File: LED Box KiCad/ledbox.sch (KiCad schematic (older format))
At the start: 23 parts

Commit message: LED Vorwiderstände auf E-Reihen angepasst
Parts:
- R?: value 185 -> 180
- R?: value 58 -> 56
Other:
- note added: "! rund 150mW !"
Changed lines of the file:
@@
 P 8300 1950
 F 0 "R?" V 8380 1950 50  0000 C CNN
-F 1 "185" V 8300 1950 50  0000 C CNN
+F 1 "180" V 8300 1950 50  0000 C CNN
 F 2 "" V 8230 1950 50  0001 C CNN
 F 3 "" H 8300 1950 50  0001 C CNN
@@
 P 8800 1950
 F 0 "R?" V 8880 1950 50  0000 C CNN
-F 1 "58" V 8800 1950 50  0000 C CNN
+F 1 "56" V 8800 1950 50  0000 C CNN
 F 2 "" V 8730 1950 50  0001 C CNN
 F 3 "" H 8800 1950 50  0001 C CNN
@@
 Wire Wire Line
 	6000 4100 6000 4000
+Text Notes 8700 2350 1    60   ~ 0
+! rund 150mW !
 $EndSCHEMATC

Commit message: Ordner plot in output geändert. BOM hinzugefügt
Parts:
- gave numbers to parts that had none: 23

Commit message: Version 1.1: - RGB LED Symbol angepasst - Button und IR LED auf eine vierer Klemmleiste Footprints assoziiert
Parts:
- removed D1: LED_IR, symbol LED
- removed D2: LED_RGB, symbol LED_RGB
- removed J2: Button, symbol Conn_01x02
- added D1: LRTBG6TG, ledbox-newfootprints:LED-6-BIG, symbol LRTBG6TG
- added J2: BTN_IR, ledbox-newfootprints:METZ-SR21304VBNC, symbol Conn_01x04
- C1, C2, C3, C4: footprint (none) -> Capacitors_SMD:C_1206
- C5: footprint (none) -> Capacitors_SMD:CP_Elec_4x5.7
- CON1: value AVR-ISP-6 -> AVR_ISP; footprint AVR-ISP-6 -> Pin_Headers:Pin_Header_Straight_2x03
- J1: value Conn_02x05_Odd_Even -> Bus; footprint (none) -> Pin_Headers:Pin_Header_Straight_2x05
- R1, R2, R3, R4, R5, R6, R7, R8, R9: footprint (none) -> Resistors_SMD:R_1206
- U1: footprint Housings_DIP:DIP-20_W7.62mm -> Housings_SOIC:SOIC-20W_7.5x12.8mm_Pitch1.27mm
- U3: footprint (none) -> Housings_SOIC:SOIC-16_3.9x9.9mm_Pitch1.27mm
- Y1: footprint (none) -> Crystals:Crystal_HC49-SD_SMD
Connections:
- net labels added: IR_LED_DRV
- wire segments 92 -> 93
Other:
- note added: "Button"
- note added: "IR LED"
- moved on the sheet: R9

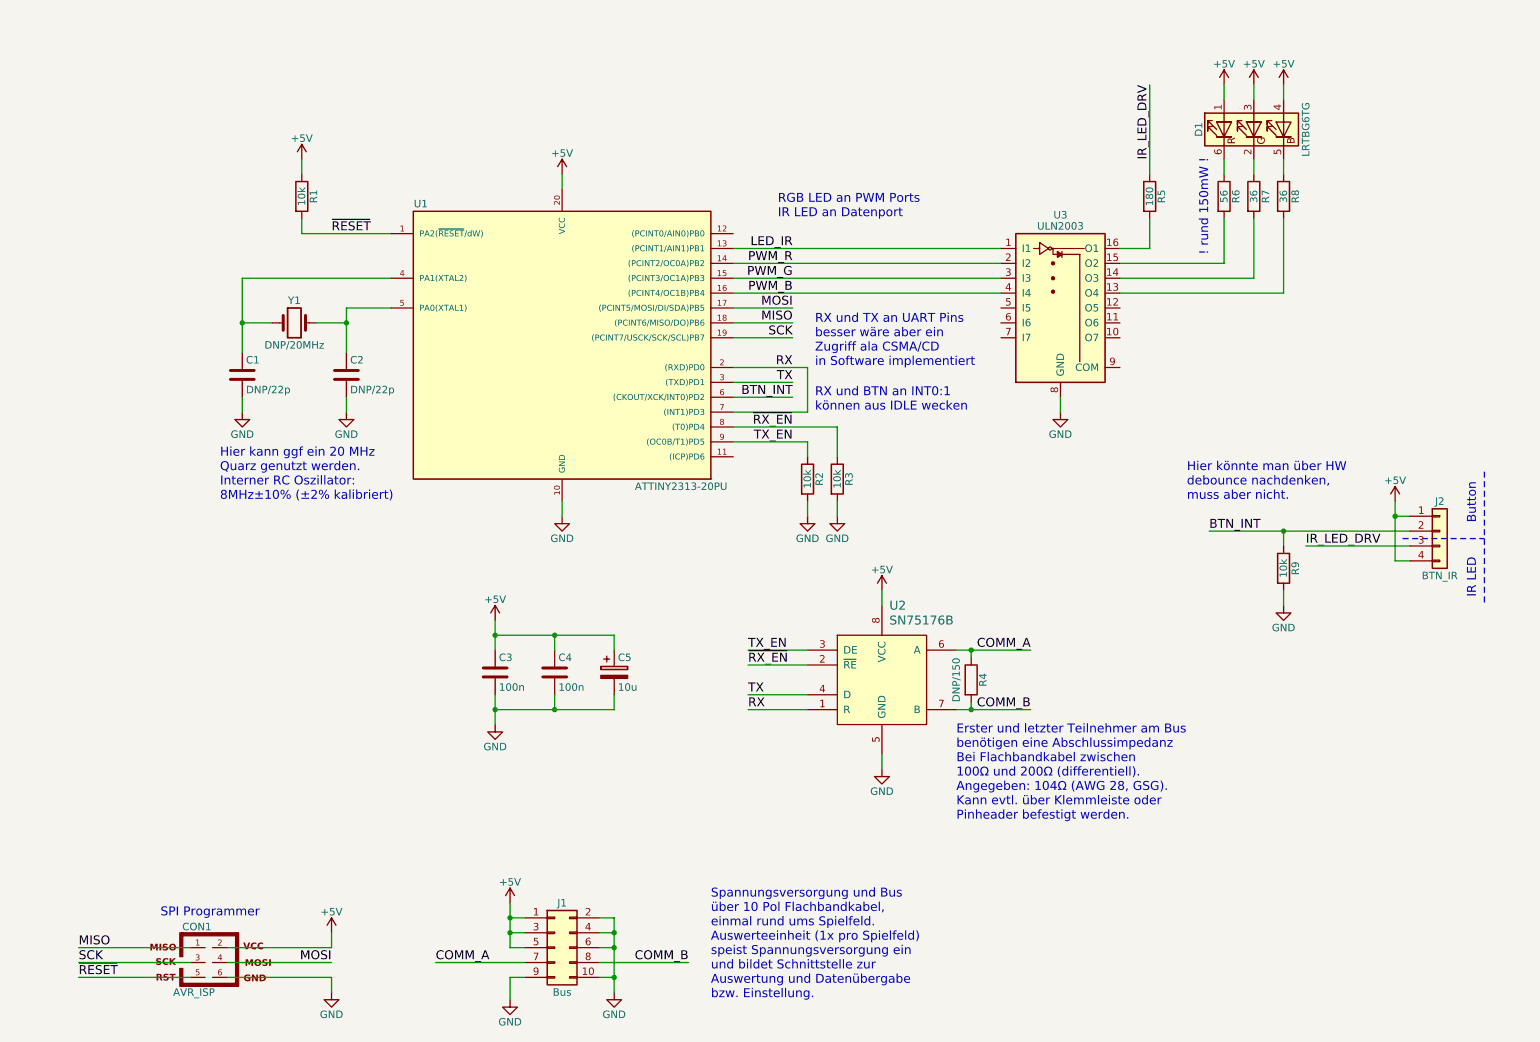
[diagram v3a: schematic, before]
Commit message: Version 2 - Anforderungen für Software hinzugefügt - CSMA/CA anstatt CSMA/CD - Kollisionsdetektion hinzugefügt - Verbinder für IR LED und Button getrennt und unterschiedlich gemacht - zusätzlicher Anschluss für Spannungsversorgung
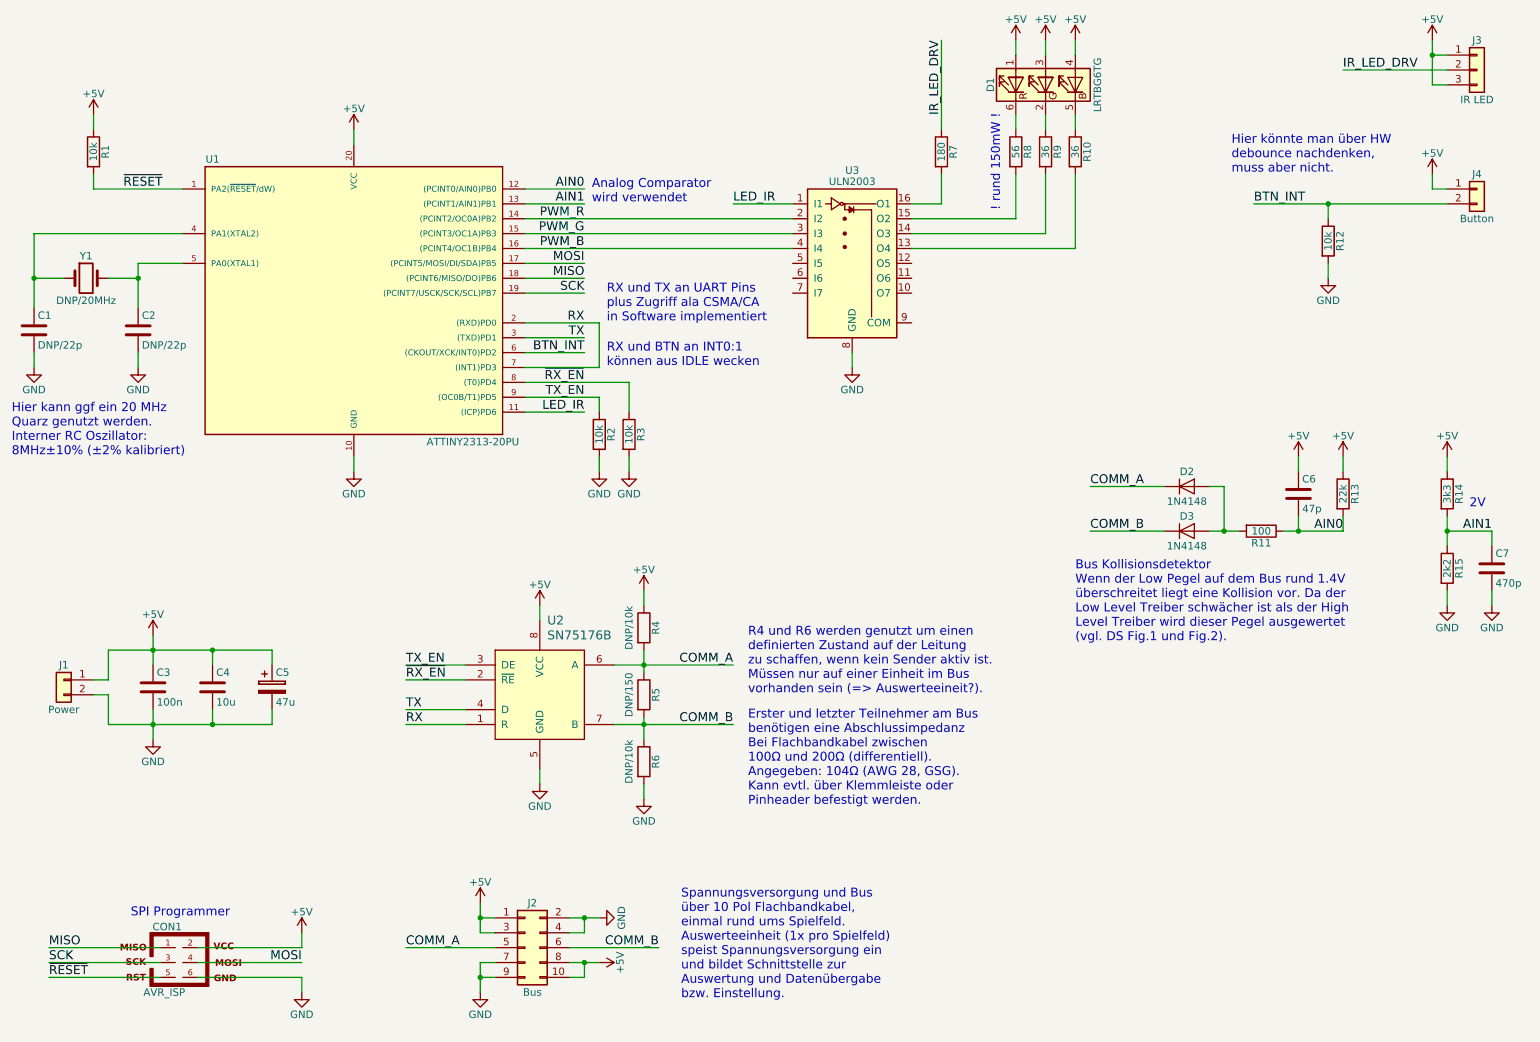
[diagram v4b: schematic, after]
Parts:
- removed J2: BTN_IR, ledbox-newfootprints:METZ-SR21304VBNC, symbol Conn_01x04
- added C6: 47p, Capacitors_SMD:C_1206, symbol C
- added C7: 470p, Capacitors_SMD:C_1206, symbol C
- added D2, D3: 1N4148, Diodes_SMD:D_MiniMELF, symbol D
- added J1: Power, Connectors_Terminal_Blocks:TerminalBlock_Pheonix_MKDS1.5-2pol, symbol Conn_01x02
- added J3: IR LED, Pin_Headers:Pin_Header_Straight_1x03, symbol Conn_01x03
- added J4: Button, Pin_Headers:Pin_Header_Straight_1x02, symbol Conn_01x02
- added R11: 100, Resistors_SMD:R_1206, symbol R
- added R13: 22k, Resistors_SMD:R_1206, symbol R
- added R14: 3k3, Resistors_SMD:R_1206, symbol R
- added R15: 2k2, Resistors_SMD:R_1206, symbol R
- added R4, R6: DNP/10k, Resistors_SMD:R_1206, symbol R
- C4: value 100n -> 10u
- C5: value 10u -> 47u
- renumbered J1 to J2, R8 to R10, R9 to R12, R4 to R5, R5 to R7, R6 to R8, R7 to R9
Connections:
- net +5V: now also J2.10 (Pin_10), J2.8 (Pin_8), C6.1, J1.1 (Pin_1), J3.1 (Pin_1), J3.3 (Pin_3), J4.1 (Pin_1), R13.1, R14.1, R4.1; no longer J2.5 (Pin_5)
- net BTN_INT: now also J4.2 (Pin_2)
- net COMM_A: now also J2.5 (Pin_5), D2.1 (K), R4.2; no longer J2.7 (Pin_7)
- net COMM_B: now also J2.6 (Pin_6), D3.1 (K), R6.1; no longer J2.8 (Pin_8)
- net GND: now also J2.7 (Pin_7), C7.2, J1.2 (Pin_2), R15.2, R6.2; no longer J2.10 (Pin_10), J2.6 (Pin_6)
- net IR_LED_DRV: now also J3.2 (Pin_2)
- net LED_IR: now also U1.11 ((ICP)PD6); no longer U1.13 ((PCINT1/AIN1)PB1)
- net AIN0: now reaches U1.12 ((PCINT0/AIN0)PB0)
- net AIN0: now also C6.2, R11.1, R13.2
- new net: D2.2 (A), D3.2 (A), R11.2
- new net AIN1: C7.1, R14.2, R15.1, U1.13 ((PCINT1/AIN1)PB1)
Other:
- note added: "2V"
- note added: "Analog Comparator \nwird verwendet"
- note added: "Bus Kollisionsdetektor\nWenn der Low Pegel auf dem Bus rund 1.4V \nüberschreitet liegt eine Kollision vor. Da der \nLow Level Treiber schwächer ist als der High \nLevel Treiber wird dieser Pegel ausgewertet \n(vgl. DS Fig.1 und Fig.2)."
- note added: "R4 und R6 werden genutzt um einen \ndefinierten Zustand auf der Leitung \nzu schaffen, wenn kein Sender aktiv ist.\nMüssen nur auf einer Einheit im Bus \nvorhanden sein (=> Auswerteeineit?)."
- note added: "RX und TX an UART Pins\nplus Zugriff ala CSMA/CA\nin Software implementiert"
- note removed: "Button"
- note removed: "IR LED"
- note removed: "RGB LED an PWM Ports\nIR LED an Datenport"
- note removed: "RX und TX an UART Pins\nbesser wäre aber ein \nZugriff ala CSMA/CD\nin Software implementiert"
- moved on the sheet: C1, C2, C3, C4, C5, CON1, D1, J2, R1, R10, R12, R2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

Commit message: Exchanged SN75176B with ST485C
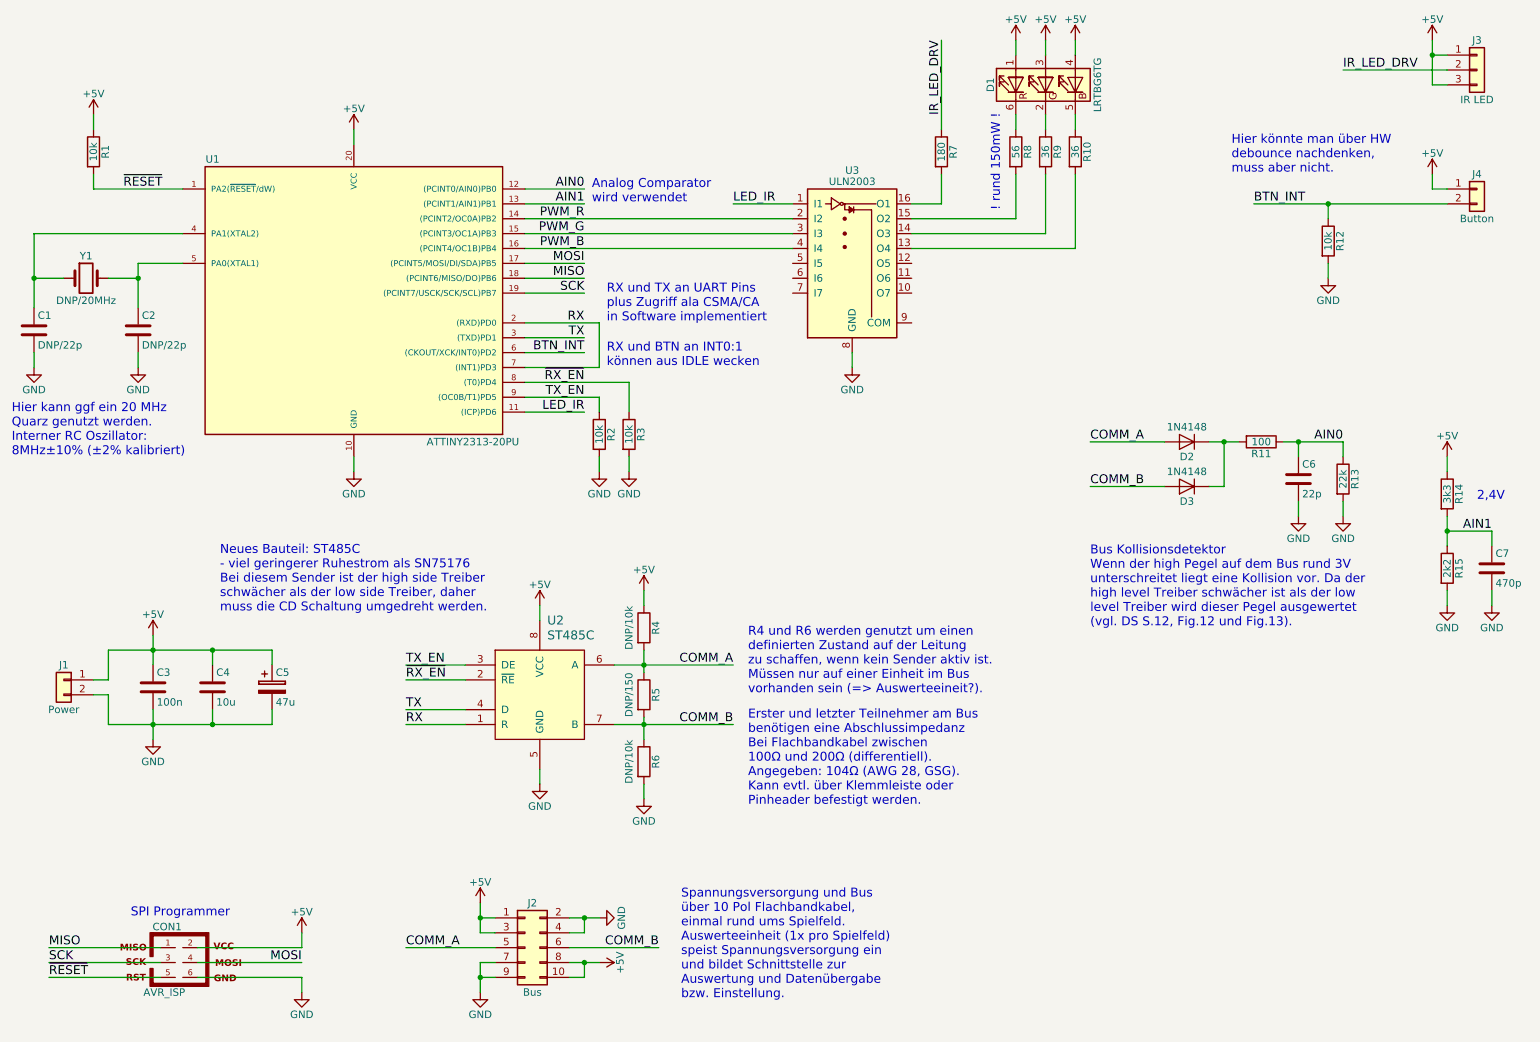
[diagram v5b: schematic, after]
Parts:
- C6: value 47p -> 22p
- U2: value SN75176B -> ST485C
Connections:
- net +5V: no longer C6.1, R13.1
- net AIN0: now also C6.1, R13.1; no longer C6.2, R13.2
- net COMM_A: now also D2.2 (A); no longer D2.1 (K)
- net COMM_B: now also D3.2 (A); no longer D3.1 (K)
- net GND: now also C6.2, R13.2
- new net: D2.1 (K), D3.1 (K), R11.2
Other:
- note added: "2,4V"
- note added: "Bus Kollisionsdetektor\nWenn der high Pegel auf dem Bus rund 3V \nunterschreitet liegt eine Kollision vor. Da der \nhigh level Treiber schwächer ist als der low \nlevel Treiber wird dieser Pegel ausgewertet \n(vgl. DS S.12, Fig.12 und Fig.13)."
- note added: "Neues Bauteil: ST485C \n- viel geringerer Ruhestrom als SN75176 \nBei diesem Sender ist der high side Treiber \nschwächer als der low side Treiber, daher \nmuss die CD Schaltung umgedreht werden.\n"
- note removed: "2V"
- note removed: "Bus Kollisionsdetektor\nWenn der Low Pegel auf dem Bus rund 1.4V \nüberschreitet liegt eine Kollision vor. Da der \nLow Level Treiber schwächer ist als der High \nLevel Treiber wird dieser Pegel ausgewertet \n(vgl. DS Fig.1 und Fig.2)."
- moved on the sheet: C6, D2, D3, R11, R13
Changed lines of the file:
@@
 P 4200 5300
 F 0 "U2" H 4250 5800 60  0000 L CNN
-F 1 "SN75176B" H 4250 5700 60  0000 L CNN
+F 1 "ST485C" H 4250 5700 60  0000 L CNN
 F 2 "Housings_SOIC:SOIC-8_3.9x4.9mm_Pitch1.27mm" H 4250 5900 60  0001 L CNN
-F 3 "http://www.ti.com/lit/ds/symlink/sn65176b.pdf" H 4250 6000 60  0001 L CNN
+F 3 "http://www.st.com/content/ccc/resource/technical/document/datasheet/4b/81/a8/cd/8a/72/47/82/CD00002183.pdf/files/CD00002183.pdf/jcr:content/translations/en.CD00002183.pdf" H 4250 6000 60  0001 L CNN
 	1    4200 5300
 	1    0    0    -1
@@
 Wire Wire Line
 	4500 3400 4100 3400
+Text Label 7900 3600 0    60   ~ 0
+COMM_A
 Text Label 7900 3900 0    60   ~ 0
-COMM_A
-Text Label 7900 4200 0    60   ~ 0
 COMM_B
 $Comp
 L D D2
 U 1 1 59D7F0C6
+P 8550 3600
+F 0 "D2" H 8550 3700 50  0000 C CNN
+F 1 "1N4148" H 8550 3500 50  0000 C CNN
+F 2 "Diodes_SMD:D_MiniMELF" H 8550 3600 50  0001 C CNN
+F 3 "" H 8550 3600 50  0001 C CNN
+	1    8550 3600
+	-1   0    0    1
+$EndComp
+$Comp
+L D D3
+U 1 1 59D7F13F
 P 8550 3900
-F 0 "D2" H 8550 4000 50  0000 C CNN
+F 0 "D3" H 8550 4000 50  0000 C CNN
 F 1 "1N4148" H 8550 3800 50  0000 C CNN
 F 2 "Diodes_SMD:D_MiniMELF" H 8550 3900 50  0001 C CNN
 F 3 "" H 8550 3900 50  0001 C CNN
 	1    8550 3900
-	1    0    0    -1
-$EndComp
-$Comp
-L D D3
-U 1 1 59D7F13F
-P 8550 4200
-F 0 "D3" H 8550 4300 50  0000 C CNN
-F 1 "1N4148" H 8550 4100 50  0000 C CNN
-F 2 "Diodes_SMD:D_MiniMELF" H 8550 4200 50  0001 C CNN
-F 3 "" H 8550 4200 50  0001 C CNN
-	1    8550 4200
-	1    0    0    -1
-$EndComp
-Wire Wire Line
-	7900 4200 8400 4200
-Wire Wire Line
-	8400 3900 7900 3900
-Wire Wire Line
-	8700 4200 8900 4200
-Wire Wire Line
-	8800 4200 8800 3900
-Wire Wire Line
-	8800 3900 8700 3900
+	-1   0    0    1
+$EndComp
+Wire Wire Line
+	7900 3900 8400 3900
+Wire Wire Line
+	8400 3600 7900 3600
+Wire Wire Line
+	8700 3900 8800 3900
+Wire Wire Line
+	8800 3900 8800 3600
+Wire Wire Line
+	8700 3600 8900 3600
 $Comp
 L R R11
 U 1 1 59D7F58B
-P 9050 4200
-F 0 "R11" V 9130 4200 50  0000 C CNN
-F 1 "100" V 9050 4200 50  0000 C CNN
-F 2 "Resistors_SMD:R_1206" V 8980 4200 50  0001 C CNN
-F 3 "" H 9050 4200 50  0001 C CNN
-	1    9050 4200
+P 9050 3600
+F 0 "R11" V 9130 3600 50  0000 C CNN
+F 1 "100" V 9050 3600 50  0000 C CNN
+F 2 "Resistors_SMD:R_1206" V 8980 3600 50  0001 C CNN
+F 3 "" H 9050 3600 50  0001 C CNN
+	1    9050 3600
 	0    1    1    0
 $EndComp
@@
 L C C6
 U 1 1 59D7F6C9
-P 9300 3950
-F 0 "C6" H 9325 4050 50  0000 L CNN
-F 1 "47p" H 9325 3850 50  0000 L CNN
-F 2 "Capacitors_SMD:C_1206" H 9338 3800 50  0001 C CNN
-F 3 "" H 9300 3950 50  0001 C CNN
-	1    9300 3950
+P 9300 3850
+F 0 "C6" H 9325 3950 50  0000 L CNN
+F 1 "22p" H 9325 3750 50  0000 L CNN
+F 2 "Capacitors_SMD:C_1206" H 9338 3700 50  0001 C CNN
+F 3 "" H 9300 3850 50  0001 C CNN
+	1    9300 3850
 	1    0    0    -1
 $EndComp
@@
 L R R13
 U 1 1 59D7F73B
-P 9600 3950
-F 0 "R13" V 9680 3950 50  0000 C CNN
-F 1 "22k" V 9600 3950 50  0000 C CNN
-F 2 "Resistors_SMD:R_1206" V 9530 3950 50  0001 C CNN
-F 3 "" H 9600 3950 50  0001 C CNN
-	1    9600 3950
-	1    0    0    -1
-$EndComp
-Text Label 9600 4200 2    60   ~ 0
+P 9600 3850
+F 0 "R13" V 9680 3850 50  0000 C CNN
+F 1 "22k" V 9600 3850 50  0000 C CNN
+F 2 "Resistors_SMD:R_1206" V 9530 3850 50  0001 C CNN
+F 3 "" H 9600 3850 50  0001 C CNN
+	1    9600 3850
+	1    0    0    -1
+$EndComp
+Text Label 9600 3600 2    60   ~ 0
 AIN0
-Text Notes 7800 4950 0    60   ~ 0
-Bus Kollisionsdetektor\nWenn der Low Pegel auf dem Bus rund 1.4V \nüberschreitet liegt eine Kollision vor. Da der \nLow Level Treiber schwächer ist als der High \nLevel Treiber wird dieser Pegel ausgewertet \n(vgl. DS Fig.1 und Fig.2).
+Text Notes 7900 4850 0    60   ~ 0
+Bus Kollisionsdetektor\nWenn der high Pegel auf dem Bus rund 3V \nunterschreitet liegt eine Kollision vor. Da der \nhigh level Treiber schwächer ist als der low \nlevel Treiber wird dieser Pegel ausgewertet \n(vgl. DS S.12, Fig.12 und Fig.13).
 $Comp
 L +5V #PWR026
@@
 Wire Wire Line
 	10300 3800 10300 3700
-Text Notes 10450 4050 0    60   ~ 0
-2V
+Text Notes 10500 4000 0    60   ~ 0
+2,4V
 $Comp
 L C C7
@@
 Wire Wire Line
 	10600 4300 10600 4200
-Connection ~ 8800 4200
-Wire Wire Line
-	9200 4200 9600 4200
-Wire Wire Line
-	9600 4200 9600 4100
-Wire Wire Line
-	9300 4200 9300 4100
-Connection ~ 9300 4200
-$Comp
-L +5V #PWR029
-U 1 1 59D83ED5
-P 9300 3700
-F 0 "#PWR029" H 9300 3550 50  0001 C CNN
-F 1 "+5V" H 9300 3840 50  0000 C CNN
-F 2 "" H 9300 3700 50  0001 C CNN
-F 3 "" H 9300 3700 50  0001 C CNN
-	1    9300 3700
-	1    0    0    -1
-$EndComp
-$Comp
-L +5V #PWR030
-U 1 1 59D83F43
-P 9600 3700
-F 0 "#PWR030" H 9600 3550 50  0001 C CNN
-F 1 "+5V" H 9600 3840 50  0000 C CNN
-F 2 "" H 9600 3700 50  0001 C CNN
-F 3 "" H 9600 3700 50  0001 C CNN
-	1    9600 3700
-	1    0    0    -1
-$EndComp
-Wire Wire Line
-	9600 3700 9600 3800
-Wire Wire Line
-	9300 3800 9300 3700
+Wire Wire Line
+	9200 3600 9600 3600
 Text Label 4500 2000 2    60   ~ 0
 AIN1
@@
 Connection ~ 4500 6800
 Wire Wire Line
-	4600 7100 4400 7100
+	4400 7100 4600 7100
 Wire Wire Line
 	4400 7200 4500 7200
@@
 Connection ~ 4500 7100
 Wire Wire Line
-	3800 7300 3800 7100
+	3800 7100 3800 7300
 Wire Wire Line
 	3800 7100 3900 7100
@@
 	1    0    0    -1
 $EndComp
+Text Notes 2050 4750 0    60   ~ 0
+Neues Bauteil: ST485C \n- viel geringerer Ruhestrom als SN75176 \nBei diesem Sender ist der high side Treiber \nschwächer als der low side Treiber, daher \nmuss die CD Schaltung umgedreht werden.\n
+Connection ~ 8800 3600
+$Comp
+L GND #PWR?
+U 1 1 59D8C75F
+P 9300 4100
+F 0 "#PWR?" H 9300 3850 50  0001 C CNN
+F 1 "GND" H 9300 3950 50  0000 C CNN
+F 2 "" H 9300 4100 50  0001 C CNN
+F 3 "" H 9300 4100 50  0001 C CNN
+	1    9300 4100
+	1    0    0    -1
+$EndComp
+$Comp
+L GND #PWR?
+U 1 1 59D8C7D0
+P 9600 4100
+F 0 "#PWR?" H 9600 3850 50  0001 C CNN
+F 1 "GND" H 9600 3950 50  0000 C CNN
+F 2 "" H 9600 4100 50  0001 C CNN
+F 3 "" H 9600 4100 50  0001 C CNN
+	1    9600 4100
+	1    0    0    -1
+$EndComp
+Wire Wire Line
+	9600 4100 9600 4000
+Wire Wire Line
+	9300 4100 9300 4000
+Wire Wire Line
+	9300 3700 9300 3600
+Connection ~ 9300 3600
+Wire Wire Line
+	9600 3600 9600 3700
 $EndSCHEMATC
